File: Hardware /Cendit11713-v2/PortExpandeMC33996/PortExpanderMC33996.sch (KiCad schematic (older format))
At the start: 4 parts

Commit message: Commit para respaldo ultima hora
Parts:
- added C? (x5): 0.1uF, symbol C
- added C?: 10uF, symbol CP
- added J? (x2): CONN_01X08, symbol CONN_01X08
- added U?: MC33996EKR2, SOIC65P1030X265-32N, symbol MC33996EKR2
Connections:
- net labels added: SO, SO_INT
- wire segments 60 -> 129

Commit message: Trabajo en CenditLab.Reducido + Cendit11713
  - CenditLab componenets GUI setup frecuencia
  - Cendit11713 esquematicos expansor puerto GPIB
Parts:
- gave numbers to parts that had none: 13
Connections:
- net labels added: SO_CHAIN
- net labels removed: SO_INT
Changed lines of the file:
@@
 LIBS:cmos4000
 LIBS:CenditBasic
-LIBS:MC33996EKR2
+LIBS:cendit-basic
+LIBS:PortExpanderMC33996-cache
 EELAYER 25 0
 EELAYER END
@@
 $EndDescr
 $Comp
-L MC33996EKR2 U?
+L MC33996EKR2 U1
 U 1 1 59BAD405
 P 2700 2350
-F 0 "U?" H 2477 3456 50  0000 L BNN
+F 0 "U1" H 2477 3456 50  0000 L BNN
 F 1 "MC33996EKR2" H 2509 981 50  0000 L BNN
 F 2 "SOIC65P1030X265-32N" H 2700 2350 50  0001 L BNN
@@
 $EndComp
 $Comp
-L CONN_01X14 J?
+L CONN_01X14 J1
 U 1 1 59BAD6CB
 P 800 2200
-F 0 "J?" H 800 2950 50  0000 C CNN
+F 0 "J1" H 800 2950 50  0000 C CNN
 F 1 "CONN_01X14" V 900 2200 50  0000 C CNN
 F 2 "" H 800 2200 50  0001 C CNN
@@
 $EndComp
 $Comp
-L GNDPWR #PWR?
+L GNDPWR #PWR4
 U 1 1 59BAD8D0
 P 1100 3050
-F 0 "#PWR?" H 1100 2850 50  0001 C CNN
+F 0 "#PWR4" H 1100 2850 50  0001 C CNN
 F 1 "GNDPWR" H 1100 2920 50  0000 C CNN
 F 2 "" H 1100 3000 50  0001 C CNN
@@
 $EndComp
 $Comp
-L GNDPWR #PWR?
+L GNDPWR #PWR8
 U 1 1 59BAD468
 P 1800 3500
-F 0 "#PWR?" H 1800 3300 50  0001 C CNN
+F 0 "#PWR8" H 1800 3300 50  0001 C CNN
 F 1 "GNDPWR" H 1800 3370 50  0000 C CNN
 F 2 "" H 1800 3450 50  0001 C CNN
@@
 $EndComp
 $Comp
-L CONN_01X08 J?
+L CONN_01X08 J2
 U 1 1 59BADB0F
 P 4250 1900
-F 0 "J?" H 4250 2350 50  0000 C CNN
+F 0 "J2" H 4250 2350 50  0000 C CNN
 F 1 "CONN_01X08" V 4350 1900 50  0000 C CNN
 F 2 "" H 4250 1900 50  0001 C CNN
@@
 $EndComp
 $Comp
-L CONN_01X08 J?
+L CONN_01X08 J3
 U 1 1 59BADB84
 P 5050 1900
-F 0 "J?" H 5050 2350 50  0000 C CNN
+F 0 "J3" H 5050 2350 50  0000 C CNN
 F 1 "CONN_01X08" V 5150 1900 50  0000 C CNN
 F 2 "" H 5050 1900 50  0001 C CNN
@@
 	3600 3050 3700 2950
 $Comp
-L VPP #PWR?
+L VPP #PWR7
 U 1 1 59BAE748
 P 1650 1400
-F 0 "#PWR?" H 1650 1250 50  0001 C CNN
+F 0 "#PWR7" H 1650 1250 50  0001 C CNN
 F 1 "VPP" H 1650 1550 50  0000 C CNN
 F 2 "" H 1650 1400 50  0001 C CNN
@@
 $EndComp
 $Comp
-L VCC #PWR?
+L VCC #PWR9
 U 1 1 59BAE764
 P 1850 1400
-F 0 "#PWR?" H 1850 1250 50  0001 C CNN
+F 0 "#PWR9" H 1850 1250 50  0001 C CNN
 F 1 "VCC" H 1850 1550 50  0000 C CNN
 F 2 "" H 1850 1400 50  0001 C CNN
@@
 	1400 2250 1000 2250
 $Comp
-L VPP #PWR?
+L VPP #PWR3
 U 1 1 59BAF1ED
 P 1100 1400
-F 0 "#PWR?" H 1100 1250 50  0001 C CNN
+F 0 "#PWR3" H 1100 1250 50  0001 C CNN
 F 1 "VPP" H 1100 1550 50  0000 C CNN
 F 2 "" H 1100 1400 50  0001 C CNN
@@
 $EndComp
 $Comp
-L VCC #PWR?
+L VCC #PWR5
 U 1 1 59BAF209
 P 1300 1400
-F 0 "#PWR?" H 1300 1250 50  0001 C CNN
+F 0 "#PWR5" H 1300 1250 50  0001 C CNN
 F 1 "VCC" H 1300 1550 50  0000 C CNN
 F 2 "" H 1300 1400 50  0001 C CNN
@@
 	1300 1650 1000 1650
 $Comp
-L MC33996EKR2 U?
+L MC33996EKR2 U2
 U 1 1 59BAF736
 P 6850 2350
-F 0 "U?" H 6627 3456 50  0000 L BNN
+F 0 "U2" H 6627 3456 50  0000 L BNN
 F 1 "MC33996EKR2" H 6659 981 50  0000 L BNN
 F 2 "SOIC65P1030X265-32N" H 6850 2350 50  0001 L BNN
@@
 $EndComp
 $Comp
-L GNDPWR #PWR?
+L GNDPWR #PWR17
 U 1 1 59BAF73C
 P 5950 3500
-F 0 "#PWR?" H 5950 3300 50  0001 C CNN
+F 0 "#PWR17" H 5950 3300 50  0001 C CNN
 F 1 "GNDPWR" H 5950 3370 50  0000 C CNN
 F 2 "" H 5950 3450 50  0001 C CNN
@@
 $EndComp
 $Comp
-L CONN_01X08 J?
+L CONN_01X08 J4
 U 1 1 59BAF742
 P 8400 1900
-F 0 "J?" H 8400 2350 50  0000 C CNN
+F 0 "J4" H 8400 2350 50  0000 C CNN
 F 1 "CONN_01X08" V 8500 1900 50  0000 C CNN
 F 2 "" H 8400 1900 50  0001 C CNN
@@
 $EndComp
 $Comp
-L CONN_01X08 J?
+L CONN_01X08 J5
 U 1 1 59BAF748
 P 9200 1900
-F 0 "J?" H 9200 2350 50  0000 C CNN
+F 0 "J5" H 9200 2350 50  0000 C CNN
 F 1 "CONN_01X08" V 9300 1900 50  0000 C CNN
 F 2 "" H 9200 1900 50  0001 C CNN
@@
 	7750 3050 7850 2950
 $Comp
-L VPP #PWR?
+L VPP #PWR16
 U 1 1 59BAF770
 P 5800 1400
-F 0 "#PWR?" H 5800 1250 50  0001 C CNN
+F 0 "#PWR16" H 5800 1250 50  0001 C CNN
 F 1 "VPP" H 5800 1550 50  0000 C CNN
 F 2 "" H 5800 1400 50  0001 C CNN
@@
 $EndComp
 $Comp
-L VCC #PWR?
+L VCC #PWR18
 U 1 1 59BAF776
 P 6000 1400
-F 0 "#PWR?" H 6000 1250 50  0001 C CNN
+F 0 "#PWR18" H 6000 1250 50  0001 C CNN
 F 1 "VCC" H 6000 1550 50  0000 C CNN
 F 2 "" H 6000 1400 50  0001 C CNN
@@
 	5750 2150 6150 2150
 Text Label 3500 3250 0    60   ~ 0
-SO_INT
+SO_CHAIN
 Wire Wire Line
 	3400 3250 3850 3250
@@
 	6150 2250 5800 2250
 Text Label 5800 2250 0    60   ~ 0
-SO_INT
+SO_CHAIN
 Entry Wire Line
 	7900 3250 8000 3150
@@
 SO
 $Comp
-L C C?
+L C C3
 U 1 1 59BB0C99
 P 2050 4800
-F 0 "C?" H 2075 4900 50  0000 L CNN
+F 0 "C3" H 2075 4900 50  0000 L CNN
 F 1 "0.1uF" H 2075 4700 50  0000 L CNN
 F 2 "" H 2088 4650 50  0001 C CNN
@@
 $EndComp
 $Comp
-L C C?
+L C C5
 U 1 1 59BB0D1E
 P 5650 4750
-F 0 "C?" H 5675 4850 50  0000 L CNN
+F 0 "C5" H 5675 4850 50  0000 L CNN
 F 1 "0.1uF" H 5675 4650 50  0000 L CNN
 F 2 "" H 5688 4600 50  0001 C CNN
@@
 $EndComp
 $Comp
-L CP C?
+L CP C1
 U 1 1 59BB0FF4
 P 950 4800
-F 0 "C?" H 975 4900 50  0000 L CNN
+F 0 "C1" H 975 4900 50  0000 L CNN
 F 1 "10uF" H 975 4700 50  0000 L CNN
 F 2 "" H 988 4650 50  0001 C CNN
@@
 $EndComp
 $Comp
-L C C?
+L C C4
 U 1 1 59BB13CD
 P 2300 4800
-F 0 "C?" H 2325 4900 50  0000 L CNN
+F 0 "C4" H 2325 4900 50  0000 L CNN
 F 1 "0.1uF" H 2325 4700 50  0000 L CNN
 F 2 "" H 2338 4650 50  0001 C CNN
@@
 $EndComp
 $Comp
-L C C?
+L C C6
 U 1 1 59BB148F
 P 6000 4750
-F 0 "C?" H 6025 4850 50  0000 L CNN
+F 0 "C6" H 6025 4850 50  0000 L CNN
 F 1 "0.1uF" H 6025 4650 50  0000 L CNN
 F 2 "" H 6038 4600 50  0001 C CNN
@@
 $EndComp
 $Comp
-L C C?
+L C C2
 U 1 1 59BB1591
 P 1300 4800
-F 0 "C?" H 1325 4900 50  0000 L CNN
+F 0 "C2" H 1325 4900 50  0000 L CNN
 F 1 "0.1uF" H 1325 4700 50  0000 L CNN
 F 2 "" H 1338 4650 50  0001 C CNN
@@
 $EndComp
 $Comp
-L GNDPWR #PWR?
+L GNDPWR #PWR2
 U 1 1 59BB1787
 P 950 5100
-F 0 "#PWR?" H 950 4900 50  0001 C CNN
+F 0 "#PWR2" H 950 4900 50  0001 C CNN
 F 1 "GNDPWR" H 950 4970 50  0000 C CNN
 F 2 "" H 950 5050 50  0001 C CNN
@@
 $EndComp
 $Comp
-L GNDPWR #PWR?
+L GNDPWR #PWR6
 U 1 1 59BB17B5
 P 1300 5100
-F 0 "#PWR?" H 1300 4900 50  0001 C CNN
+F 0 "#PWR6" H 1300 4900 50  0001 C CNN
 F 1 "GNDPWR" H 1300 4970 50  0000 C CNN
 F 2 "" H 1300 5050 50  0001 C CNN
@@
 $EndComp
 $Comp
-L GNDPWR #PWR?
+L GNDPWR #PWR11
 U 1 1 59BB17E3
 P 2050 5150
-F 0 "#PWR?" H 2050 4950 50  0001 C CNN
+F 0 "#PWR11" H 2050 4950 50  0001 C CNN
 F 1 "GNDPWR" H 1950 5000 50  0000 C CNN
 F 2 "" H 2050 5100 50  0001 C CNN
@@
 $EndComp
 $Comp
-L GNDPWR #PWR?
+L GNDPWR #PWR13
 U 1 1 59BB185F
 P 2300 5150
-F 0 "#PWR?" H 2300 4950 50  0001 C CNN
+F 0 "#PWR13" H 2300 4950 50  0001 C CNN
 F 1 "GNDPWR" H 2300 5020 50  0000 C CNN
 F 2 "" H 2300 5100 50  0001 C CNN
@@
 $EndComp
 $Comp
-L GNDPWR #PWR?
+L GNDPWR #PWR15
 U 1 1 59BB18CE
 P 5650 5100
-F 0 "#PWR?" H 5650 4900 50  0001 C CNN
+F 0 "#PWR15" H 5650 4900 50  0001 C CNN
 F 1 "GNDPWR" H 5650 4970 50  0000 C CNN
 F 2 "" H 5650 5050 50  0001 C CNN
@@
 $EndComp
 $Comp
-L GNDPWR #PWR?
+L GNDPWR #PWR20
 U 1 1 59BB18FC
 P 6000 5100
-F 0 "#PWR?" H 6000 4900 50  0001 C CNN
+F 0 "#PWR20" H 6000 4900 50  0001 C CNN
 F 1 "GNDPWR" H 6000 4970 50  0000 C CNN
 F 2 "" H 6000 5050 50  0001 C CNN
@@
 $EndComp
 $Comp
-L VPP #PWR?
+L VPP #PWR1
 U 1 1 59BB1C36
 P 950 4350
-F 0 "#PWR?" H 950 4200 50  0001 C CNN
+F 0 "#PWR1" H 950 4200 50  0001 C CNN
 F 1 "VPP" H 950 4500 50  0000 C CNN
 F 2 "" H 950 4350 50  0001 C CNN
@@
 $EndComp
 $Comp
-L VPP #PWR?
+L VPP #PWR10
 U 1 1 59BB1C98
 P 2050 4350
-F 0 "#PWR?" H 2050 4200 50  0001 C CNN
+F 0 "#PWR10" H 2050 4200 50  0001 C CNN
 F 1 "VPP" H 2050 4500 50  0000 C CNN
 F 2 "" H 2050 4350 50  0001 C CNN
@@
 $EndComp
 $Comp
-L VCC #PWR?
+L VCC #PWR12
 U 1 1 59BB1D21
 P 2300 4350
-F 0 "#PWR?" H 2300 4200 50  0001 C CNN
+F 0 "#PWR12" H 2300 4200 50  0001 C CNN
 F 1 "VCC" H 2300 4500 50  0000 C CNN
 F 2 "" H 2300 4350 50  0001 C CNN
@@
 $EndComp
 $Comp
-L VCC #PWR?
+L VCC #PWR19
 U 1 1 59BB1E0C
 P 6000 4350
-F 0 "#PWR?" H 6000 4200 50  0001 C CNN
+F 0 "#PWR19" H 6000 4200 50  0001 C CNN
 F 1 "VCC" H 6000 4500 50  0000 C CNN
 F 2 "" H 6000 4350 50  0001 C CNN
@@
 $EndComp
 $Comp
-L VPP #PWR?
+L VPP #PWR14
 U 1 1 59BB1E3A
 P 5650 4350
-F 0 "#PWR?" H 5650 4200 50  0001 C CNN
+F 0 "#PWR14" H 5650 4200 50  0001 C CNN
 F 1 "VPP" H 5650 4500 50  0000 C CNN
 F 2 "" H 5650 4350 50  0001 C CNN

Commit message: Cendit11713: Trabajo en esquematicos + PCB
  - Se editan esquematicos expansor IO Viking
  - Creada tarjeta PCB adaptador multipuertos
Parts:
- removed J1: CONN_01X14, symbol CONN_01X14
- removed J2, J3, J4, J5: CONN_01X08, symbol CONN_01X08
- added C3: 10uF, symbol CP
- added CONN1: VIKING_SPI_BUS, symbol VIKING_SPI_BUS
- added CONN2, CONN3: VIKING_HEADER, symbol VIKING_HEADER
- added J?: DEBUG_CONN, symbol CONN_01X10
- renumbered C3 to C4, C4 to C5, C5 to C6, C6 to C7
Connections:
- net labels added: /CSX, /CSY, /RESET, MISO, MOSI, PWM, PX0, PX1, PX10, PX11, PX12, PX13, PX14, PX15, PX2, PX3, PX4, PX5, PX6, PX7, PX8, PX9, PY0, PY1, PY10, PY11, PY12, PY13, PY14, PY15, PY2, PY3, PY4, PY5, PY6, PY7, PY8, PY9, SCLK
- net labels removed: SO, SO_CHAIN
- wire segments 129 -> 151
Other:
- moved on the sheet: C1, C2, C4, C5, C6, C7, U1, U2

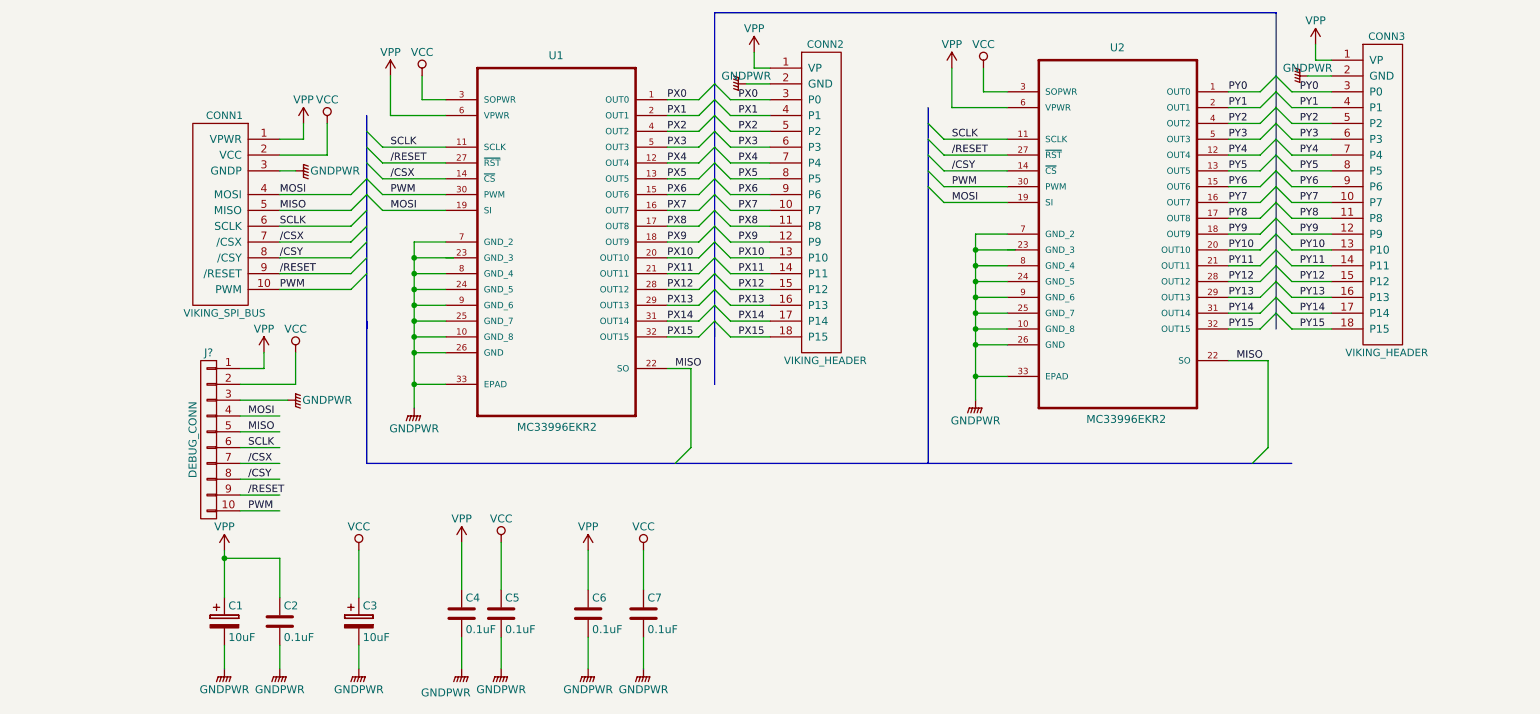
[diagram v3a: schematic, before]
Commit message: Trabajo en CenditLab.Reducido + Cendit17713 PCB
  - Clases paneles UI modificados
  - Clases para manejo y validacion de datos
  - PCB expansor puertos Viking
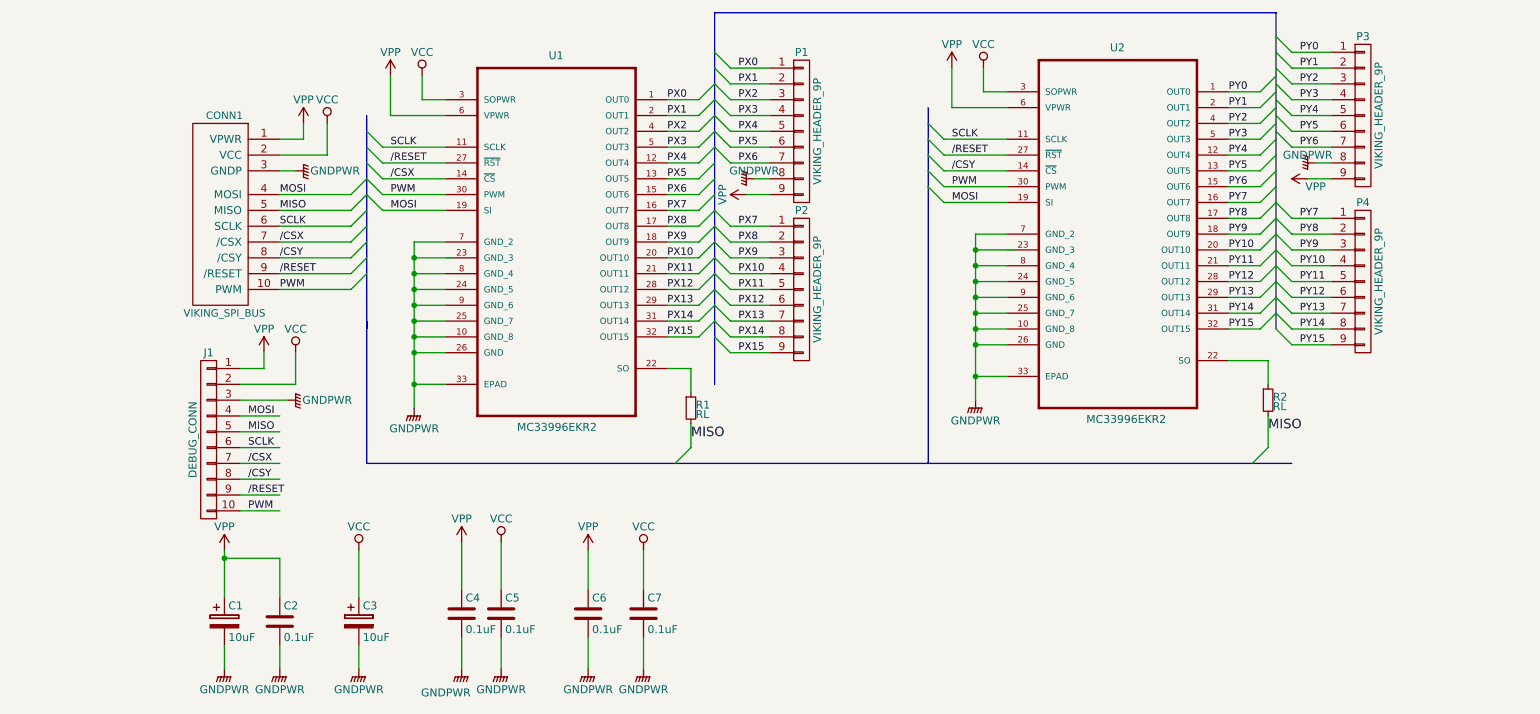
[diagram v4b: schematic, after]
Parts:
- removed CONN2, CONN3: VIKING_HEADER, symbol VIKING_HEADER
- added P1, P2, P3, P4: VIKING_HEADER_9P, Pin_Headers:Pin_Header_Straight_1x09, symbol CONN_01X09
- added R1, R2: RL, Resistors_SMD:R_0805_HandSoldering, symbol R_Small
- C1, C3: footprint (none) -> Capacitors_SMD:c_elec_3x5.3
- C2, C4, C5, C6, C7: footprint (none) -> Capacitors_SMD:C_0805_HandSoldering
- CONN1: footprint (none) -> CenditFootprints:SLIMLINE_SATA_PLUG_7P_6P
- J1: renamed from J?; footprint (none) -> Pin_Headers:Pin_Header_Straight_1x10
- U1, U2: footprint SOIC65P1030X265-32N -> LibreriaKicad:MC33996EKR2

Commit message: Trabajo en Cendit11713
  - Revision de esquematicos + PCBs
  - Generacion de archivos Gerber
  - CapacitiveKeyboard -> edicion PCB
  - Inicia PCB GpibPortExpander
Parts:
- CONN1: symbol VIKING_SPI_BUS -> VIKING_SPI_BUS-RESCUE-PortExpanderMC33996
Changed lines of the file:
@@
 EESchema Schematic File Version 2
+LIBS:PortExpanderMC33996-rescue
 LIBS:adc-dac
 LIBS:memory
@@
 PY15
 $Comp
-L VIKING_SPI_BUS CONN1
+L VIKING_SPI_BUS-RESCUE-PortExpanderMC33996 CONN1
 U 1 1 59DD0DB3
 P 1300 2900
